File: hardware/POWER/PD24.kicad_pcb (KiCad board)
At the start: 2 copper layers, 39.7 x 14 mm, 21 parts, among them J1 USB_C_Receptacle_USB2.0_16P, J2 Conn_01x02_Pin, J4 Conn_01x08_Pin, J5 Conn_01x12_Pin, U1 HUSB238, U2 SY7304

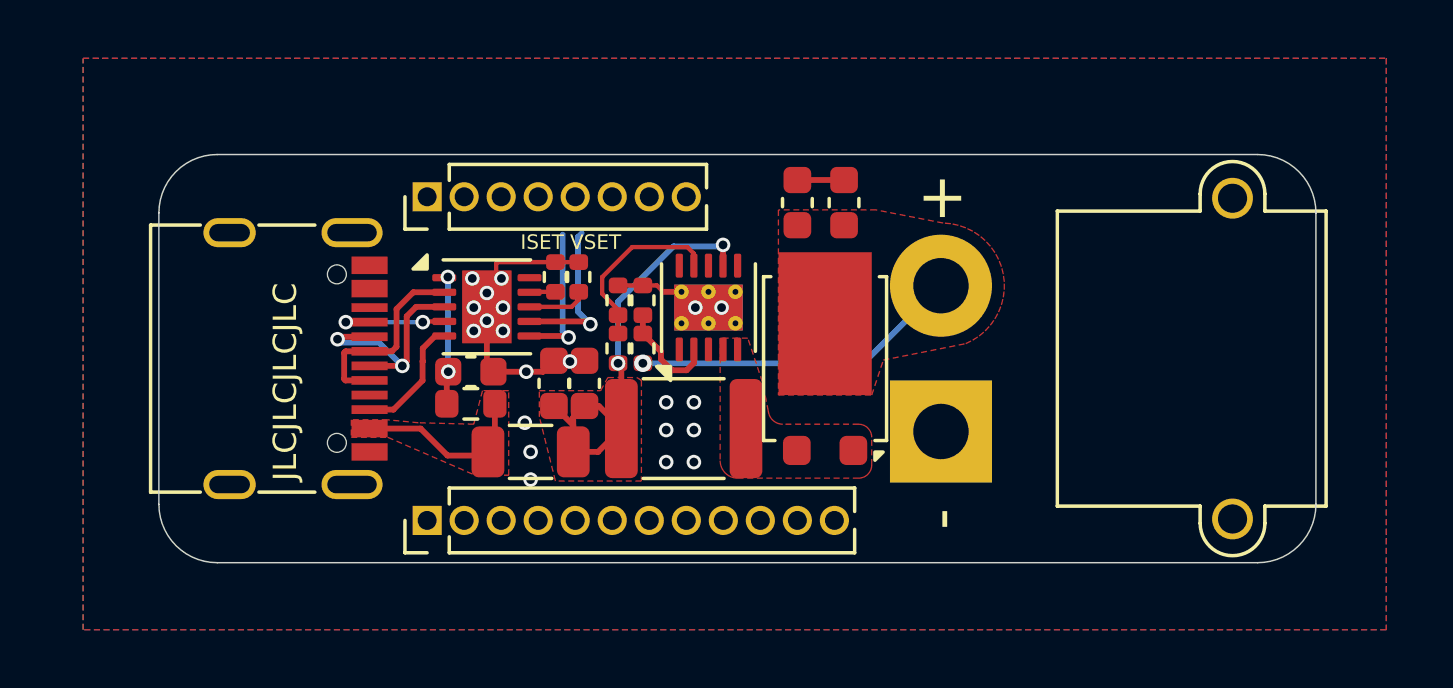
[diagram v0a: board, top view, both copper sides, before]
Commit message: 进一步优化了布局，减少了分叉，使大电流的回流路径更短
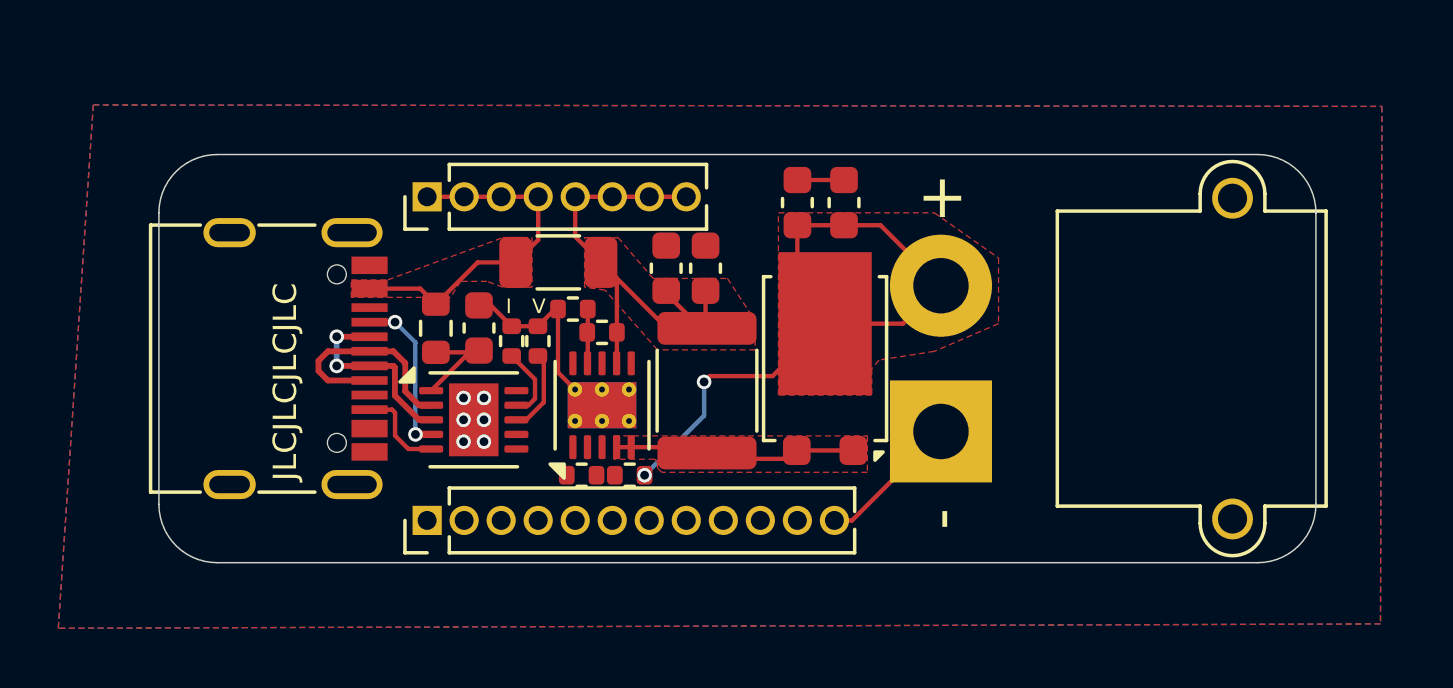
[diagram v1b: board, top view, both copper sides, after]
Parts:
- moved R8 6.57 mm to (127.2, 99.7)
- moved R5 6.36 mm to (128.0, 107.0), turned to 180 degrees
- moved C3 5.73 mm to (132.2, 99.9)
- moved C2 5.52 mm to (130.9, 99.9)
- moved U2 4.95 mm to (128.7, 104.6)
- moved R2 4.37 mm to (129.7, 107.0), turned to 180 degrees
- moved U1 3.90 mm to (124.3, 105.1)
- moved R1 2.85 mm to (123.0, 102.0), turned to -90 degrees
- moved R4 2.66 mm to (125.6, 102.4)
- moved R7 2.61 mm to (126.5, 102.4)
- moved R6 1.58 mm to (127.7, 101.3), turned to 180 degrees
- moved L1 1.53 mm to (132.3, 104.1), turned to -90 degrees
- moved C1 1.53 mm to (124.5, 102.0), turned to 90 degrees
- moved R3 0.78 mm to (128.7, 102.1), turned to 180 degrees
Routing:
- net +24V: track 11.3 -> 23.1 mm, vias 1 -> 2
- net /SY7304-24v/SW: track 0.00 -> 8.40 mm
- net /VBUS: track 6.25 -> 12.2 mm
- net /SCL: track 5.47 -> 0.00 mm, vias 1 -> 0
- net /SDA: track 4.84 -> 0.00 mm, vias 1 -> 0
- net Net-(U2-EN): track 6.24 -> 1.87 mm
- net Net-(U2-FB): track 3.62 -> 0.00 mm
- net Net-(U1-ISET): track 0.89 -> 2.53 mm
- net /VIN-: track 16.7 -> 18.2 mm, vias 2 -> 0
- net GND: track 14.3 -> 12.8 mm, vias 21 -> 6
- net /HUSB238/D-: track 8.04 -> 6.70 mm
- net /HUSB238/CC1: track 4.33 -> 5.55 mm
- net /HUSB238/CC2: track 4.25 -> 3.13 mm
- net Net-(U1-VSET): track 2.06 -> 2.86 mm
- net /HUSB238/D+: track 6.84 -> 7.57 mm
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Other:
- board text added: "I"
- board text added: "V"
- board text removed: "ISET"
- board text removed: "VSET"

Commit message: 更换升压方案为同步整流，较大降低了升压电路的发热量，将acc和ldo放在电源板上
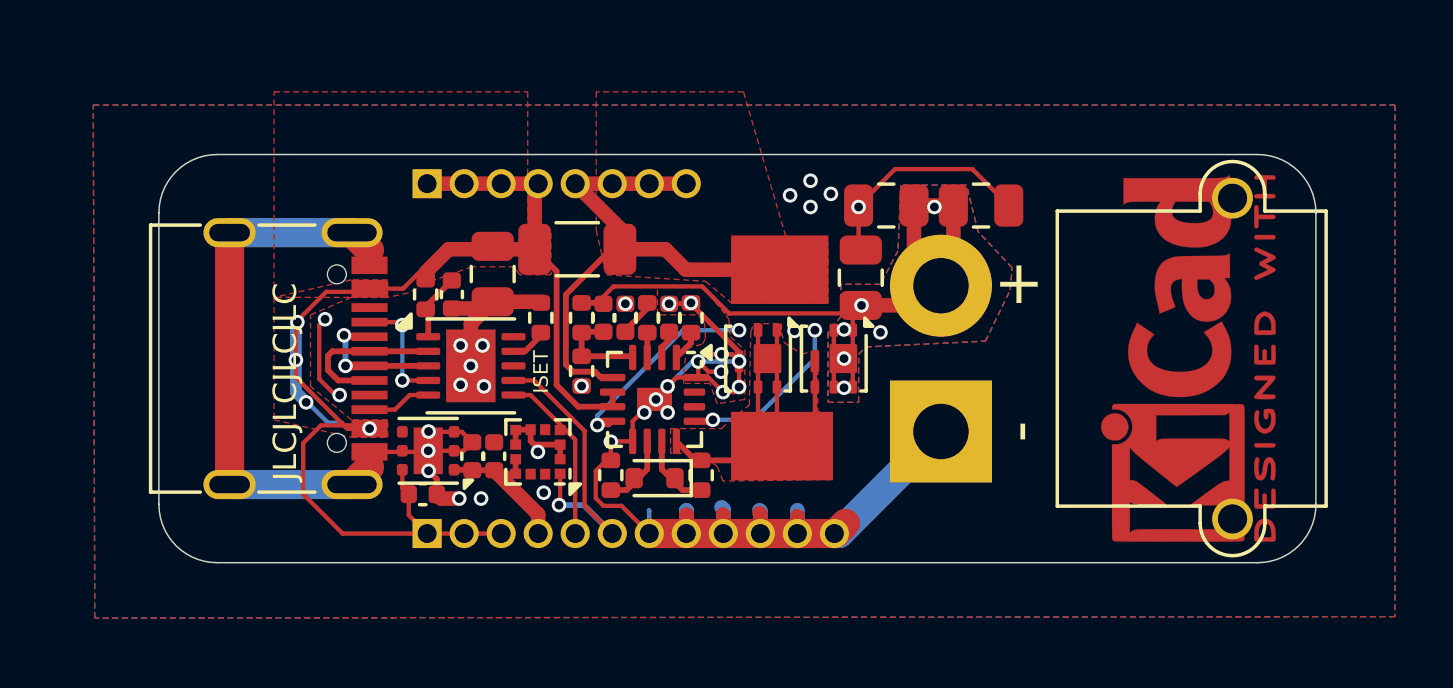
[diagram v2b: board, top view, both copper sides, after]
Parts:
- removed the R2 at (129.7, 107.0)
- removed R3: 100K, Resistor_SMD:R_0402_1005Metric
- added C10: 15nF, Capacitor_SMD:C_0402_1005Metric, F.Cu at (129.5, 101.6)
- added C11: 1uF, Capacitor_SMD:C_0402_1005Metric, F.Cu at (122.5, 107.7)
- added C12: 2.2uF, Capacitor_SMD:C_0402_1005Metric, F.Cu at (124.2, 106.3)
- added C13: 33pF, Capacitor_SMD:C_0402_1005Metric, F.Cu at (128.8, 101.6)
- added C6: 10uF, Capacitor_SMD:C_0805_2012Metric, F.Cu at (137.6, 100.2)
- added C7: 10uF, Capacitor_SMD:C_0805_2012Metric, F.Cu at (138.4, 97.8)
- added C8: 10uF, Capacitor_SMD:C_0805_2012Metric, F.Cu at (141.7, 97.8)
- added C9: 100nF, Capacitor_SMD:C_0402_1005Metric, F.Cu at (131.0, 101.6)
- added Q1: CSD17313Q2, Package_SON:Texas_DQK, F.Cu at (136.7, 103.0)
- added Q2: CSD17313Q2, Package_SON:Texas_DQK, F.Cu at (134.1, 103.0)
- added R1: 20mR, Resistor_SMD:R_1206_3216Metric, F.Cu at (127.8, 99.2)
- added SYMBOL1: 符号, Symbol:KiCad-Logo2_5mm_Copper, F.Cu at (148.8, 103.0)
- added SYMBOL2: 符号, Symbol:OSHW-Symbol_8.9x8mm_SilkScreen, B.Cu at (118.3, 102.9)
- added SYMBOL3: 符号, Symbol:ESD-Logo_6.6x6mm_SilkScreen, B.Cu at (127.3, 102.9)
- added U3: TPS43060RTE, Package_DFN_QFN:Texas_RTE_WQFN-16-1EP_3x3mm_P0.5mm_EP1.2x0.8mm, F.Cu at (130.5, 104.4)
- added U4: TPS709-WSON-6, Package_SON:WSON-6-1EP_2x2mm_P0.65mm_EP1x1.6mm, F.Cu at (122.7, 106.2)
- C1: footprint Capacitor_SMD:C_0603_1608Metric -> Capacitor_SMD:C_0402_1005Metric
- C2: value 10uF -> 100nF; footprint Capacitor_SMD:C_0603_1608Metric -> Capacitor_SMD:C_0402_1005Metric
- C3: value 1uF -> 100nF; footprint Capacitor_SMD:C_0603_1608Metric -> Resistor_SMD:R_0402_1005Metric
- C4: value 22uF -> 10uF; footprint Capacitor_SMD:C_0603_1608Metric -> Capacitor_SMD:C_0805_2012Metric
- C5: value 22uF -> 4.7uF; footprint Capacitor_SMD:C_0603_1608Metric -> Resistor_SMD:R_0402_1005Metric
- D1: value D_Schottky -> 1N4148WT; footprint Package_TO_SOT_SMD:TO-277B -> Diode_SMD:D_SOD-523
- L1: value 4.7uH -> L; footprint Inductor_SMD:L_1812_4532Metric -> Inductor_SMD:L_Sunlord_MWSA0618S
- R2: renamed from R1; footprint Resistor_SMD:R_0603_1608Metric -> Resistor_SMD:R_0402_1005Metric
- R5: value 5.1K -> 200K
- R6: value 20k -> 7.5K
- R7: value NC -> 76.8K
- R8: value 20mR -> 10.7K; footprint Resistor_SMD:R_1206_3216Metric -> Resistor_SMD:R_0402_1005Metric
- U2: value SY7304 -> LIS2DW12; footprint Package_DFN_QFN:DFN-10-1EP_3x3mm_P0.5mm_EP1.58x2.35mm_ThermalVias -> Package_LGA:LGA-12_2x2mm_P0.5mm
- moved C4 12.3 mm to (125.0, 100.1), turned to -90 degrees
- moved C5 11.3 mm to (129.0, 107.0)
- moved C2 8.74 mm to (125.0, 106.3)
- moved D1 7.14 mm to (130.5, 107.1)
- moved C3 7.10 mm to (132.1, 107.0), turned to -90 degrees
- moved R5 5.40 mm to (128.0, 101.6), turned to -90 degrees
- moved R7 5.31 mm to (131.8, 101.6)
- moved R8 3.81 mm to (128.0, 103.4), turned to 90 degrees
- moved L1 2.81 mm to (134.9, 103.0)
- moved U2 2.72 mm to (126.5, 106.2), turned to 180 degrees
- moved R6 2.57 mm to (130.2, 101.6), turned to 90 degrees
- moved U1 1.85 mm to (124.2, 103.2)
- moved C1 1.48 mm to (123.5, 100.8), turned to -90 degrees
- moved R4 1.28 mm to (126.6, 101.6)
- moved R2 1.21 mm to (122.7, 100.8)
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- renumbered J2 to J1, J1 to J2, J4 to J3, J5 to J4
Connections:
- C2 pad 1: /VIN- -> /+3V3
- C3 pad 1: /VIN- -> /TPS43060-24V/SW
- C3 pad 2: GND -> /TPS43060-24V/BOOT
- C4 pad 1: +24V -> /VBUS
- C5 pad 1: +24V -> /TPS43060-24V/VCC
- D1 pad 1: +24V -> /TPS43060-24V/BOOT
- D1 pad 2: /SY7304-24v/SW -> /TPS43060-24V/VCC
- J4 pad 4: /VBUS -> /+3V3
- J4 pad 5: /VBUS -> /SDA
- J4 pad 6: /SDA -> /SCL
- J4 pad 7: /SCL -> GND
- L1 pad 2: /SY7304-24v/SW -> /TPS43060-24V/SW
- R5 pad 1: Net-(U2-FB) -> +24V
- R5 pad 2: GND -> Net-(U3-FB)
- R6 pad 1: Net-(U2-EN) -> Net-(U3-COMP)
- R6 pad 2: GND -> Net-(C10-Pad1)
- R7 pad 1: Net-(U1-VSET) -> Net-(U3-RT/CLK)
- R8 pad 1: /VBUS -> GND
- R8 pad 2: /VIN- -> Net-(U3-FB)
- U2 pad 1: unconnected-(U2-NC-Pad1) -> /SCL
- U2 pad 10: unconnected-(U2-NC-Pad10) -> /+3V3
- U2 pad 11: GND -> /LIS2DW12/INT2
- U2 pad 2: Net-(U2-FB) -> GND
- U2 pad 3: unconnected-(U2-NC-Pad3) -> GND
- U2 pad 4: /SY7304-24v/SW -> /SDA
- U2 pad 5: /SY7304-24v/SW -> unconnected-(U2-NC-Pad5)
- U2 pad 6: unconnected-(U2-NC-Pad6) -> GND
- U2 pad 7: /VIN- -> GND
- U2 pad 8: unconnected-(U2-NC-Pad8) -> GND
- U2 pad 9: Net-(U2-EN) -> /+3V3
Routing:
- net GND: track 12.8 -> 89.1 mm, vias 6 -> 35
- net /VBUS: track 12.2 -> 48.1 mm, vias 0 -> 4
- net /TPS43060-24V/SW: track 0.00 -> 16.9 mm
- net /SCL: track 0.00 -> 10.4 mm, vias 0 -> 1
- net /SY7304-24v/SW: track 8.40 -> 0.00 mm
- net Net-(Q2-G): track 0.00 -> 6.97 mm, vias 0 -> 2
- net /SDA: track 0.00 -> 6.43 mm
- net Net-(Q1-G): track 0.00 -> 5.93 mm, vias 0 -> 2
- net /+3V3: track 0.00 -> 5.63 mm
- net Net-(U3-FB): track 0.00 -> 3.34 mm
- net +24V: track 23.1 -> 26.1 mm, vias 2 -> 6
- net /TPS43060-24V/BOOT: track 0.00 -> 2.61 mm
- net Net-(U1-VSET): track 2.86 -> 0.28 mm
- net /TPS43060-24V/VCC: track 0.00 -> 2.51 mm
- net /HUSB238/D+: track 7.57 -> 5.57 mm
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- added copper zone on B.Cu, net +24V
- added copper zone on F.Cu, net /TPS43060-24V/SW
- removed copper zone on F.Cu, net /SY7304-24v/SW
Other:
- board text added: "ISET"
- board text removed: "I"
- board text removed: "V"

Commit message: 硬件版本v2，待验证
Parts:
- C3, C5: footprint Resistor_SMD:R_0402_1005Metric -> Capacitor_SMD:C_0402_1005Metric
- C4, C6, C7, C8: footprint Capacitor_SMD:C_0805_2012Metric -> Capacitor_SMD:C_0603_1608Metric
- R7: value 76.8K -> 78.7K
- moved SYMBOL1 2.80 mm to (146.0, 103.0)
- moved C7 0.15 mm to (138.6, 97.8)
- moved C8 0.10 mm to (141.6, 97.8)
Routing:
- net GND: vias 35 -> 36
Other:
- board text added: "PD24"
- board text added: "高压 危险 勿碰 器件"
- board text removed: "高压危险 勿碰器件"

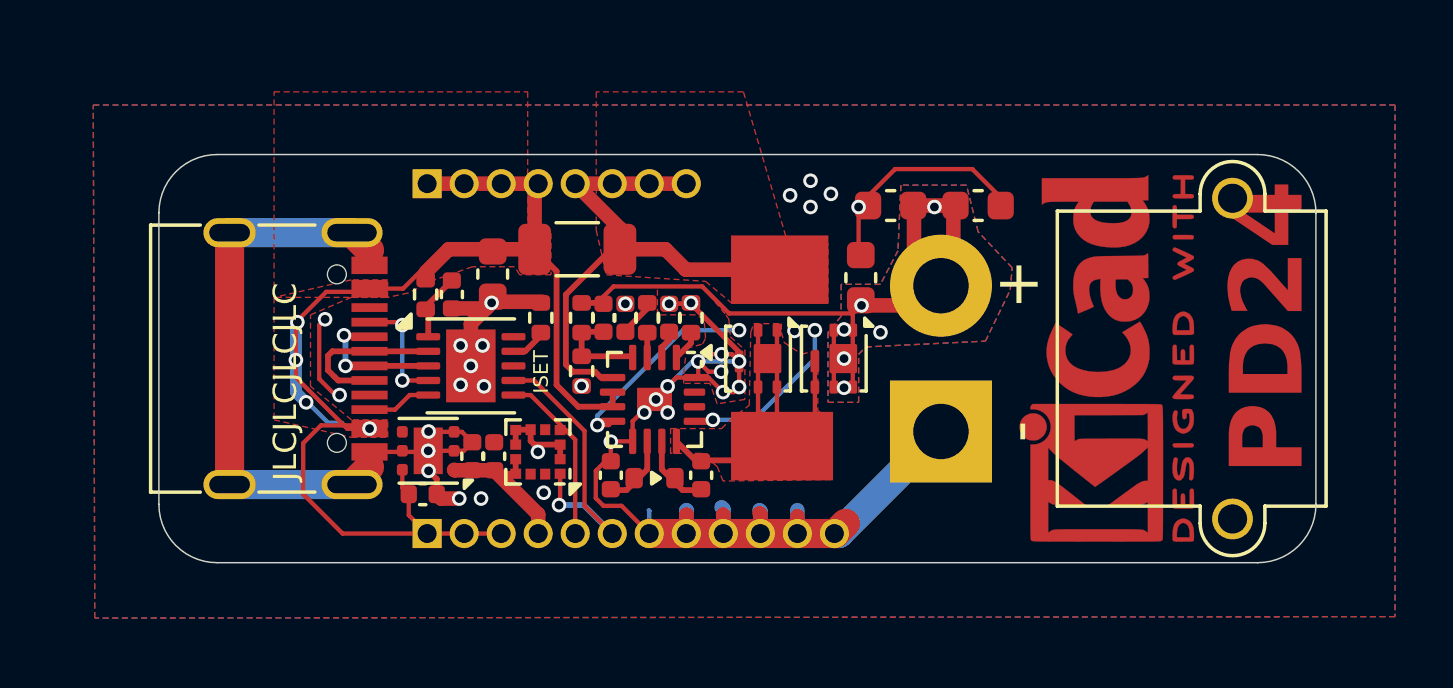
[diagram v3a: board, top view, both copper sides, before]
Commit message: lis2dw12由于错误配置了cs脚，导致进入了spi模式，但电路设计上为iic的连接方式，无法读取方向，现在已经修正，但是代码设置成了固定方向。同步升压整流确实降低了不少发热，但是好像添加的ldo由于oled电流较大，带来的额外热量更多，之后可能还是考虑使用dcdc降压
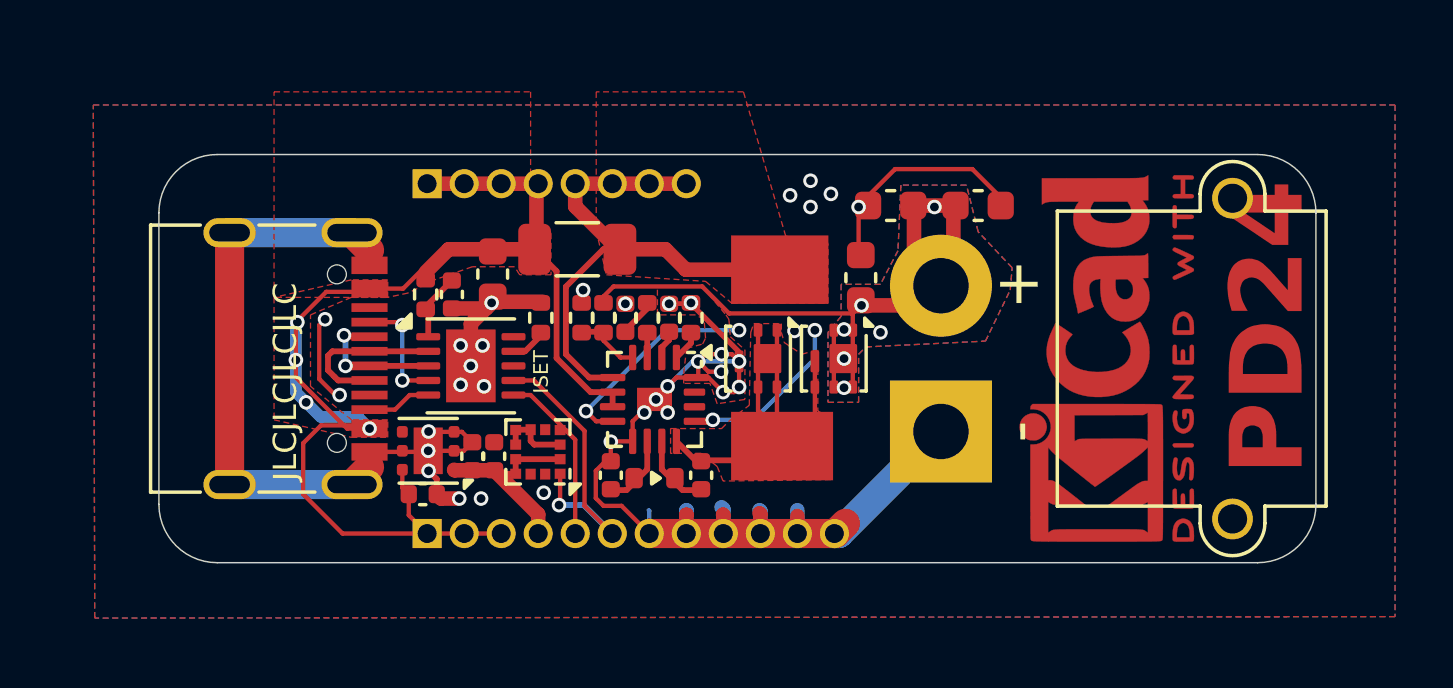
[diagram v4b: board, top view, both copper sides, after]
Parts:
- removed C13: 33pF, Capacitor_SMD:C_0402_1005Metric
- moved R8 1.83 mm to (128.0, 101.6), turned to -90 degrees
- moved R5 0.75 mm to (128.8, 101.6)
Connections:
- U2 pad 2: GND -> /+3V3
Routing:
- net /+3V3: track 5.30 -> 6.82 mm
- net Net-(U3-FB): track 3.34 -> 2.27 mm
- net /VBUS: track 48.1 -> 47.3 mm
- net +24V: track 26.1 -> 25.4 mm
- net GND: track 89.1 -> 88.6 mm, vias 36 -> 35
